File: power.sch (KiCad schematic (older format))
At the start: 40 parts, among them J1 USB_B_Mini, U1 USBLC6-2SC6, U2 BQ24190, U4 LP38691SD-3.3

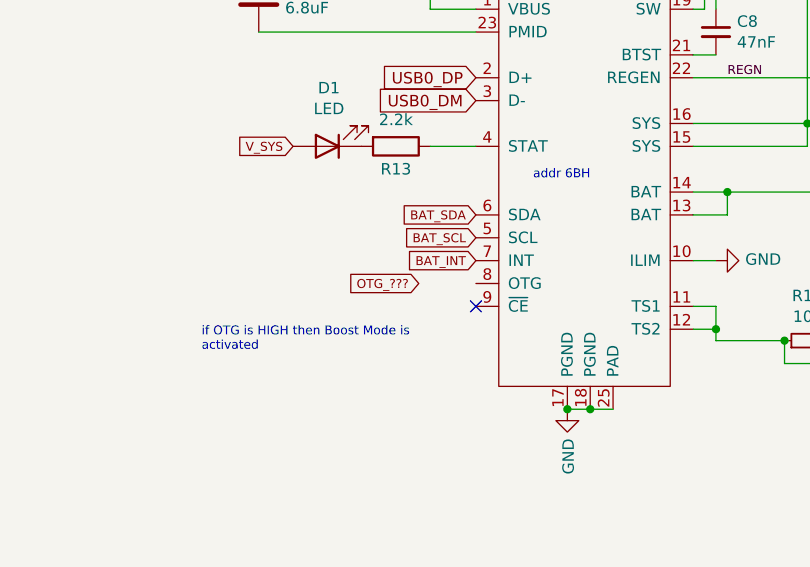
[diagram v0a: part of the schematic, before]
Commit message: Wire the OTG pin
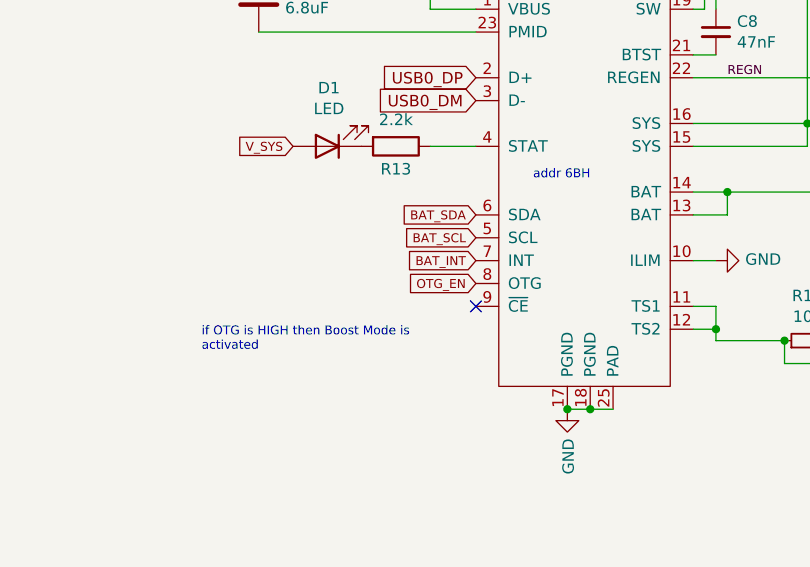
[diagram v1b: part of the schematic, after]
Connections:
- net OTG_EN: now reaches U2.8 (OTG)
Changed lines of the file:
@@
 	1900 10900 1800 10900
 Connection ~ 1800 10900
-Text GLabel 6000 5050 0    39   Input ~ 0
-OTG_???
+Text GLabel 6250 5050 0    39   Input ~ 0
+OTG_EN
 $EndSCHEMATC

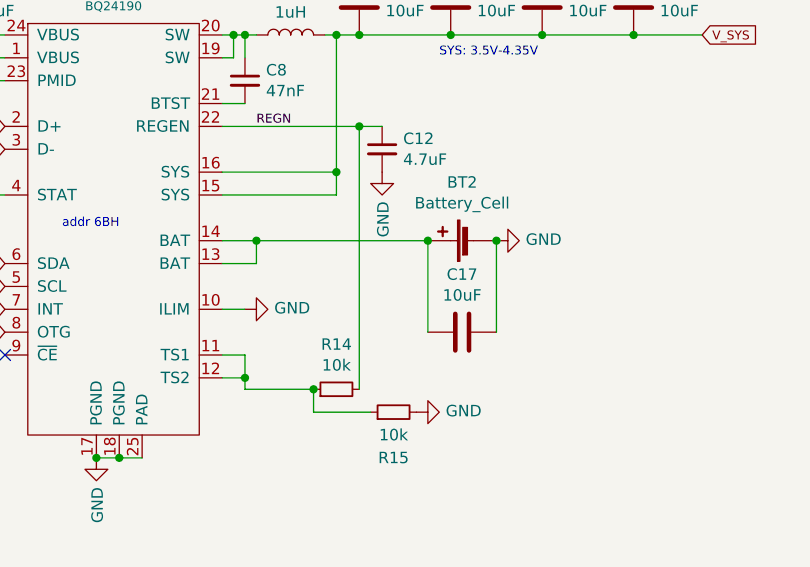
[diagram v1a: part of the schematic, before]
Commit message: Add TPs
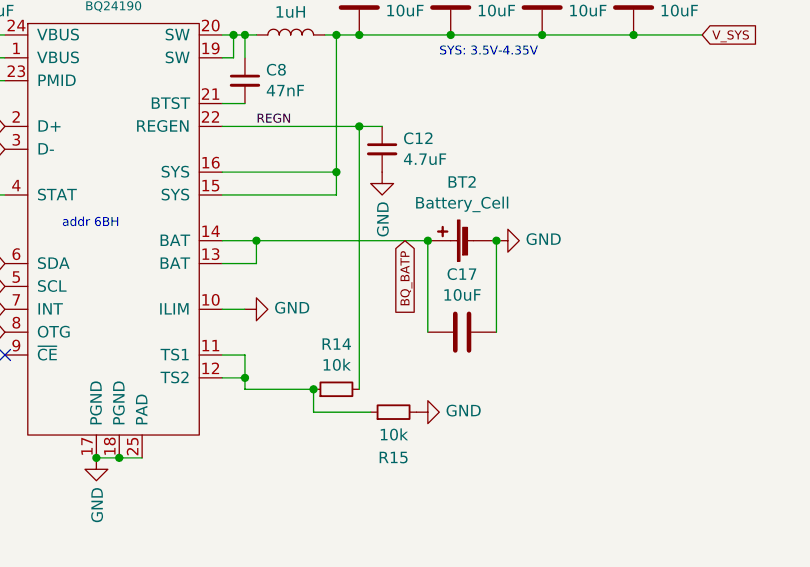
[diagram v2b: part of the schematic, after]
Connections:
- net BQ_BATP: now reaches BT2.1 (+), C17.2, U2.13 (BAT), U2.14 (BAT)
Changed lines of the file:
@@
 Text GLabel 6250 5050 0    39   Input ~ 0
 OTG_EN
+Text GLabel 8000 4650 3    39   Input ~ 0
+BQ_BATP
 $EndSCHEMATC

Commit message: Use libs; start assigning footprints
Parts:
- BT2: footprint (none) -> Connector_JST:JST_PH_B2B-PH-K_1x02_P2.00mm_Vertical
- J1: footprint (none) -> Connector_USB:USB_Mini-B_Wuerth_65100516121_Horizontal
- U1: footprint Package_TO_SOT_SMD:SOT-23-6 -> Package_TO_SOT_SMD:SOT-23-6_Handsoldering
- U2: footprint (none) -> Package_DFN_QFN:VQFN-24-1EP_4x4mm_P0.5mm_EP2.45x2.45mm_ThermalVias
- U4: footprint Package_QFP:LQFP-144_20x20mm_P0.5mm -> Package_SON:WSON-6-1EP_3x3mm_P0.95mm
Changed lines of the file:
@@
 F 0 "J1" H 1157 4867 50  0000 C CNN
 F 1 "USB_B_Mini" H 1157 4776 50  0000 C CNN
-F 2 "" H 1250 4350 50  0001 C CNN
+F 2 "Connector_USB:USB_Mini-B_Wuerth_65100516121_Horizontal" H 1250 4350 50  0001 C CNN
 F 3 "~" H 1250 4350 50  0001 C CNN
 	1    1100 4400
@@
 F 0 "U4" H 7300 1692 50  0000 C CNN
 F 1 "LP38691SD-3.3" H 7300 1601 50  0000 C CNN
-F 2 "Package_QFP:LQFP-144_20x20mm_P0.5mm" H 7300 1350 50  0001 C CNN
+F 2 "Package_SON:WSON-6-1EP_3x3mm_P0.95mm" H 7300 1350 50  0001 C CNN
 F 3 "https://www.nxp.com/docs/en/data-sheet/K66P144M180SF5V2.pdf" H 7300 1350 50  0001 C CNN
 	1    7300 1350
@@
 F 0 "U1" V 3150 4300 50  0000 L CNN
 F 1 "USBLC6-2SC6" V 2150 4150 50  0000 L CNN
-F 2 "Package_TO_SOT_SMD:SOT-23-6" H 2650 3950 50  0001 C CNN
+F 2 "Package_TO_SOT_SMD:SOT-23-6_Handsoldering" H 2650 3950 50  0001 C CNN
 F 3 "https://www.st.com/resource/en/datasheet/usblc6-2.pdf" H 2850 4800 50  0001 C CNN
 	1    2650 4450
@@
 F 0 "U2" H 6725 3751 39  0000 C CNN
 F 1 "BQ24190" H 6725 3676 39  0000 C CNN
-F 2 "" H 5700 3950 39  0001 C CNN
+F 2 "Package_DFN_QFN:VQFN-24-1EP_4x4mm_P0.5mm_EP2.45x2.45mm_ThermalVias" H 5700 3950 39  0001 C CNN
 F 3 "" H 5700 3950 39  0001 C CNN
 	1    6750 3650
@@
 F 0 "BT2" V 8555 4700 50  0000 C CNN
 F 1 "Battery_Cell" V 8464 4700 50  0000 C CNN
-F 2 "" V 8300 4710 50  0001 C CNN
+F 2 "Connector_JST:JST_PH_B2B-PH-K_1x02_P2.00mm_Vertical" V 8300 4710 50  0001 C CNN
 F 3 "~" V 8300 4710 50  0001 C CNN
 	1    8300 4650

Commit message: Assigning footprints
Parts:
- removed D2, D3: 1A, symbol Device:D_Schottky
- BT1: footprint (none) -> Battery:BatteryHolder_Keystone_1060_1x2032; mouser (none) -> 534-1060TR
- C1, C11, C12, C13, C15, C16, C17, C18, C19, C2, C20, C21, C22, C23, C24, C25, C26, C4, C5, C6, C7, C8, C9: footprint (none) -> Capacitor_SMD:C_0805_2012Metric_Pad1.18x1.45mm_HandSolder
- F1: footprint (none) -> Fuse:Fuse_0805_2012Metric_Pad1.15x1.40mm_HandSolder; mouser (none) -> 576-0805L020YR
- JP1: footprint (none) -> Jumper:SolderJumper-3_P1.3mm_Bridged2Bar12_Pad1.0x1.5mm_NumberLabels
- L1: footprint (none) -> Inductor_SMD:L_0805_2012Metric_Pad1.05x1.20mm_HandSolder; mouser (none) -> 704-MCQ1V2012-1R0-R
- R1, R13, R14, R15, R6: footprint (none) -> Resistor_SMD:R_0805_2012Metric_Pad1.20x1.40mm_HandSolder
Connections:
- net at C5.1, U4.1 (IN), U4.6 (IN): now also F1.1
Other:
- moved on the sheet: F1

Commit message: Finish led magic
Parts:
- D1: footprint (none) -> LED_SMD:LED_0603_1608Metric_Pad1.05x0.95mm_HandSolder; mouser (none) -> 859-LTST-C190GKT
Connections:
- net V_SYS: now also R13.2; no longer D1.2 (A)
- net at U2.4 (STAT): now also D1.1 (K); no longer R13.1
- new net: D1.2 (A), R13.1
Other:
- moved on the sheet: D1, R13
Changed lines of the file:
@@
 L Device:LED D?
 U 1 1 60D3B575
-P 5600 4450
+P 5750 4450
 AR Path="/5F7C29DF/60D3B575" Ref="D?"  Part="1"
 AR Path="/60CFD8F5/60D3B575" Ref="D1"  Part="1"
-F 0 "D1" H 5593 4195 50  0000 C CNN
-F 1 "LED" H 5593 4286 50  0000 C CNN
-F 2 "" H 5600 4450 50  0001 C CNN
-F 3 "~" H 5600 4450 50  0001 C CNN
-	1    5600 4450
+F 0 "D1" H 5743 4195 50  0000 C CNN
+F 1 "LED" H 5743 4286 50  0000 C CNN
+F 2 "LED_SMD:LED_0603_1608Metric_Pad1.05x0.95mm_HandSolder" H 5750 4450 50  0001 C CNN
+F 3 "~" H 5750 4450 50  0001 C CNN
+F 4 "859-LTST-C190GKT" H 5750 4450 50  0001 C CNN "mouser"
+	1    5750 4450
 	-1   0    0    1
 $EndComp
-Text GLabel 5450 4450 0    39   Input ~ 0
+Text GLabel 5300 4450 0    39   Input ~ 0
 V_SYS
 $Comp
 L Device:R R?
 U 1 1 60D3B57C
-P 5900 4450
+P 5450 4450
 AR Path="/5F7C29DF/60D3B57C" Ref="R?"  Part="1"
 AR Path="/60CFD8F5/60D3B57C" Ref="R13"  Part="1"
-F 0 "R13" V 6000 4450 50  0000 C CNN
-F 1 "2.2k" V 5784 4450 50  0000 C CNN
-F 2 "Resistor_SMD:R_0805_2012Metric_Pad1.20x1.40mm_HandSolder" V 5830 4450 50  0001 C CNN
-F 3 "~" H 5900 4450 50  0001 C CNN
-	1    5900 4450
+F 0 "R13" V 5550 4450 50  0000 C CNN
+F 1 "2.2k" V 5334 4450 50  0000 C CNN
+F 2 "Resistor_SMD:R_0805_2012Metric_Pad1.20x1.40mm_HandSolder" V 5380 4450 50  0001 C CNN
+F 3 "~" H 5450 4450 50  0001 C CNN
+	1    5450 4450
 	0    1    1    0
 $EndComp
 Wire Wire Line
-	6050 4450 6250 4450
+	5900 4450 6250 4450
 Wire Wire Line
 	7200 4750 7350 4750

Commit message: Switch keyboard matrix input to a mcp23017
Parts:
- U1: lcsc (none) -> C7519
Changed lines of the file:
@@
 F 2 "Package_TO_SOT_SMD:SOT-23-6_Handsoldering" H 2650 3950 50  0001 C CNN
 F 3 "https://www.st.com/resource/en/datasheet/usblc6-2.pdf" H 2850 4800 50  0001 C CNN
+F 4 "C7519" H 2650 4450 50  0001 C CNN "lcsc"
 	1    2650 4450
 	0    1    -1   0

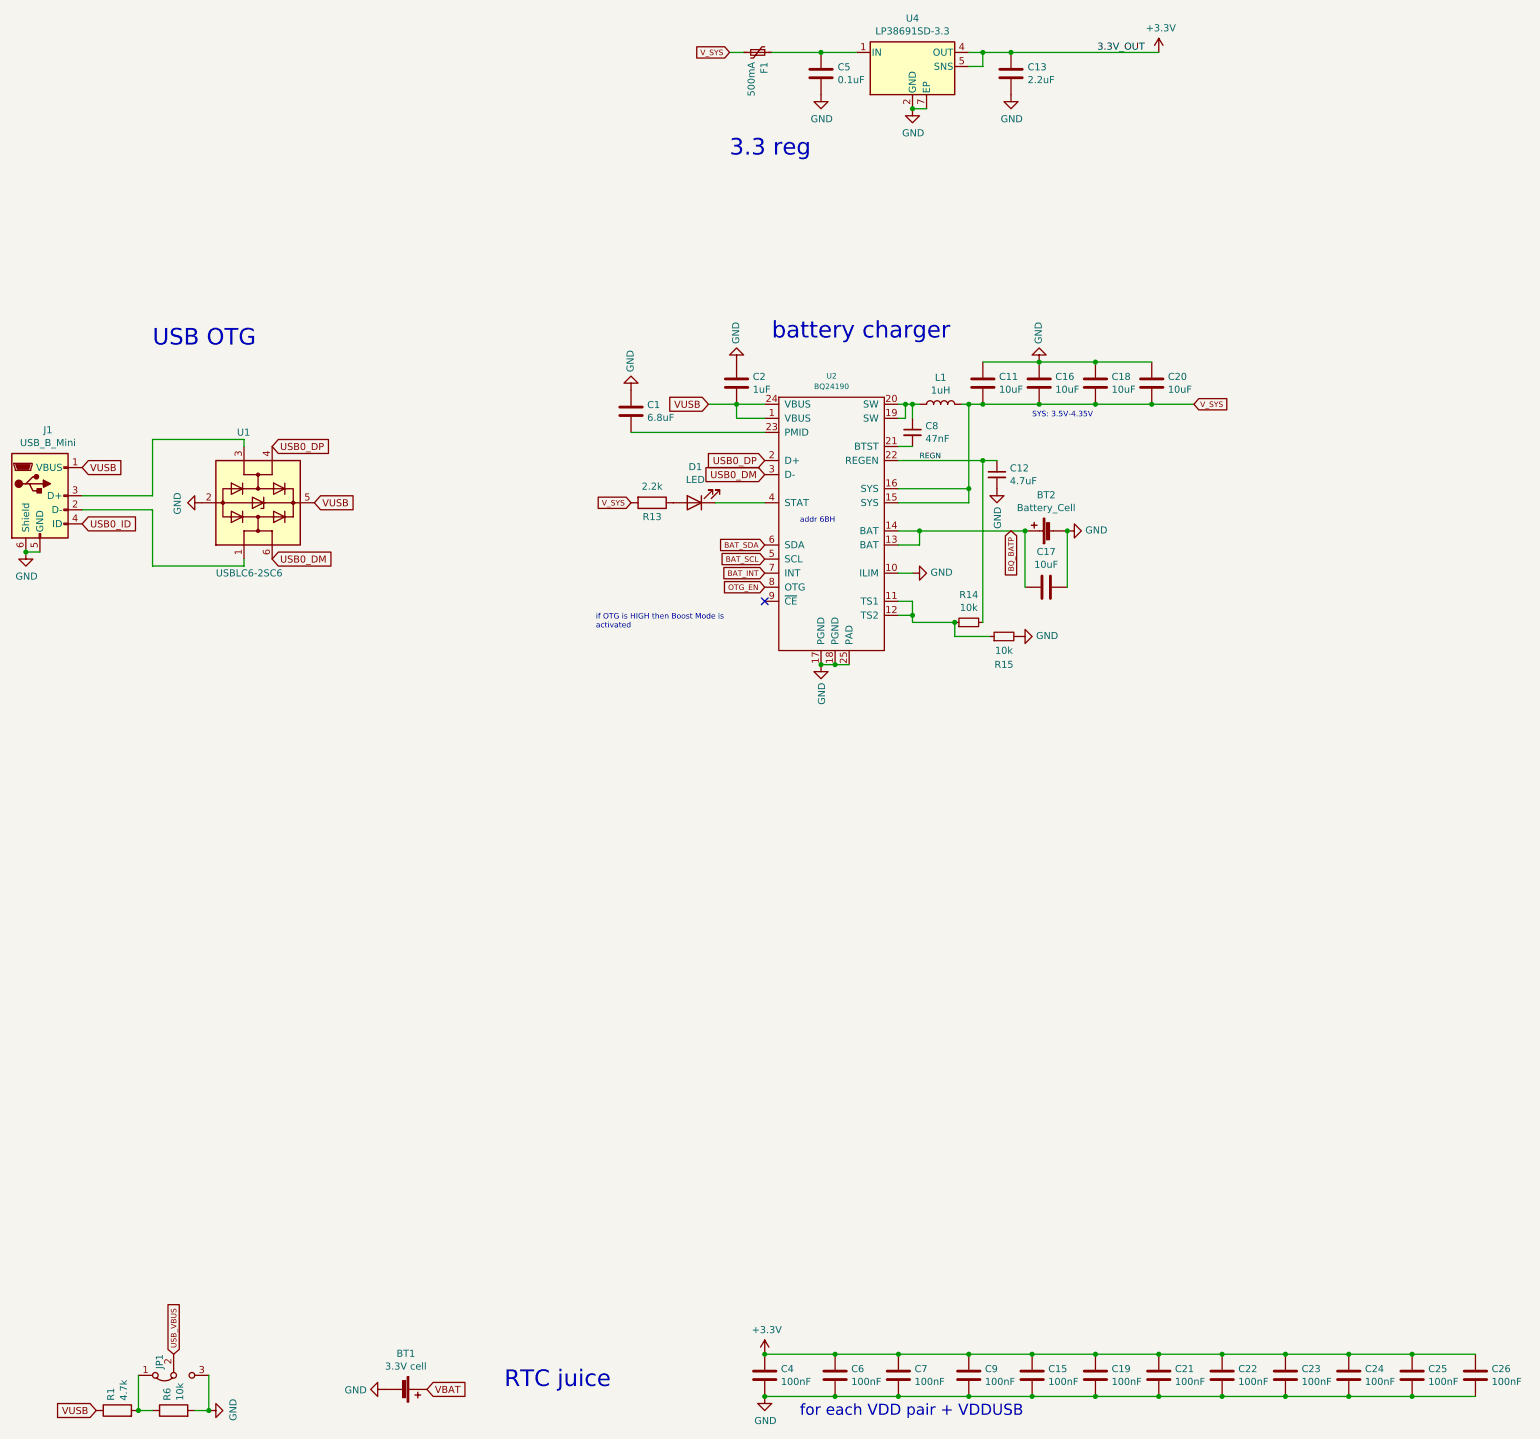
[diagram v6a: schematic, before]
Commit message: Switch stuff around; Use two MCP
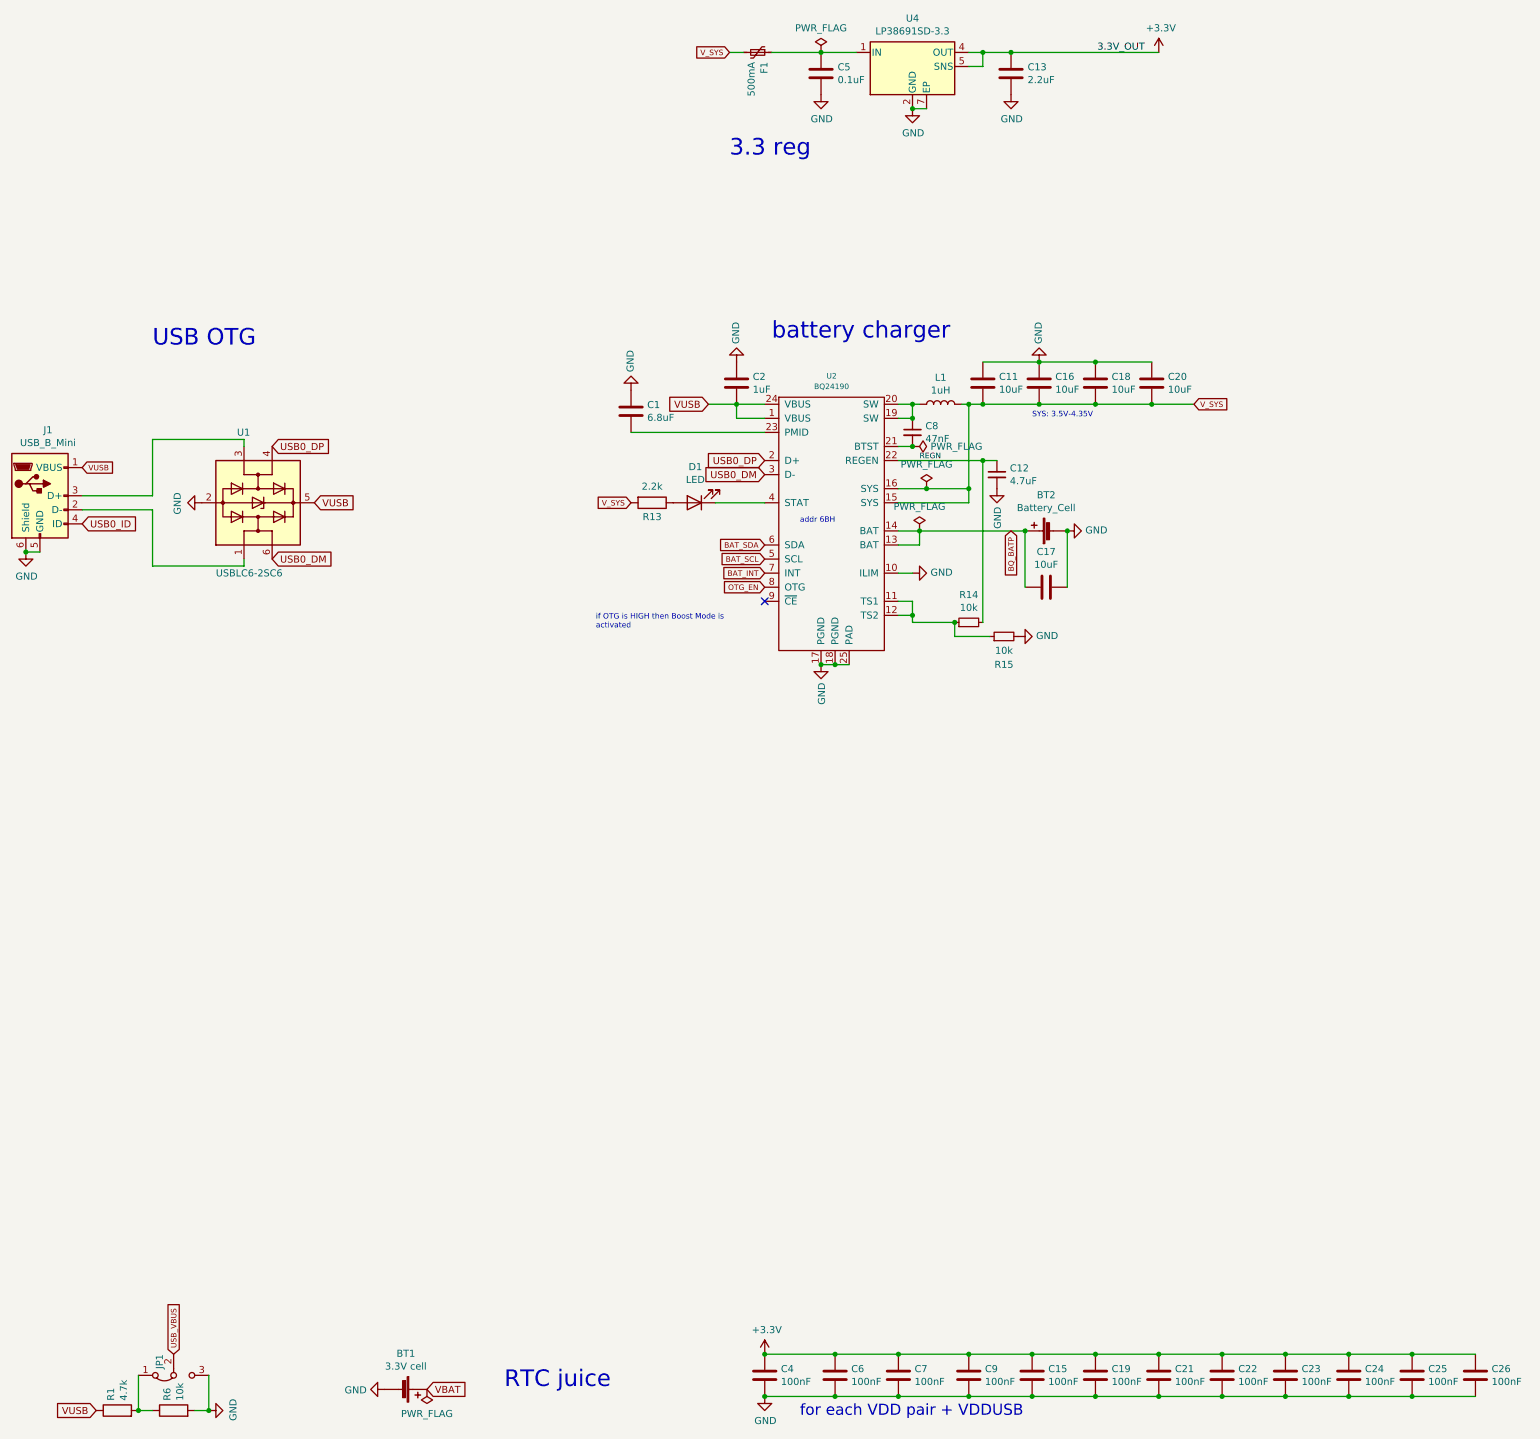
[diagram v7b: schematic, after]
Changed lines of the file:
@@
 $EndComp
-Wire Wire Line
-	6650 1250 6900 1250
 Wire Wire Line
 	7700 1350 7800 1350
 Wire Wire Line
 	7800 1350 7800 1250
-Wire Wire Line
-	7800 1250 7700 1250
-Wire Wire Line
-	7800 1250 8000 1250
 Connection ~ 7800 1250
 Connection ~ 8000 1250
@@
 	1000 4800 1100 4800
 Connection ~ 1000 4800
-Text GLabel 1400 4200 2    50   Input ~ 0
-VUSB
 Text GLabel 5850 3750 0    50   Input ~ 0
 VUSB
@@
 	1    0    0    -1
 $EndComp
-Wire Wire Line
-	5850 3750 6050 3750
 Connection ~ 6050 3750
 $Comp
@@
 	9000 3750 8600 3750
 Wire Wire Line
-	7350 3750 7300 3750
-Wire Wire Line
 	9000 3450 8600 3450
 Connection ~ 8200 3450
@@
 Text GLabel 6000 1250 0    39   Input ~ 0
 V_SYS
-$Comp
-L Device:C_Small C?
-U 1 1 60D3B51D
-P 7300 3950
-AR Path="/5F7C29DF/60D3B51D" Ref="C?"  Part="1"
-AR Path="/60CFD8F5/60D3B51D" Ref="C8"  Part="1"
-F 0 "C8" H 7392 3996 50  0000 L CNN
-F 1 "47nF" H 7392 3905 50  0000 L CNN
-F 2 "Capacitor_SMD:C_0805_2012Metric_Pad1.18x1.45mm_HandSolder" H 7300 3950 50  0001 C CNN
-F 3 "~" H 7300 3950 50  0001 C CNN
-	1    7300 3950
-	1    0    0    -1
-$EndComp
-Wire Wire Line
-	7300 3850 7300 3750
-Connection ~ 7300 3750
-Wire Wire Line
-	7300 3750 7250 3750
 Wire Wire Line
 	7200 4050 7300 4050
@@
 $EndComp
 Wire Wire Line
-	7200 4350 7700 4350
+	7200 4350 7400 4350
 Wire Wire Line
 	7700 4350 7700 3750
@@
 Wire Wire Line
 	7700 3750 7650 3750
-Wire Wire Line
-	7200 3850 7250 3850
-Wire Wire Line
-	7250 3850 7250 3750
-Connection ~ 7250 3750
-Wire Wire Line
-	7250 3750 7200 3750
 Wire Wire Line
 	7200 4450 7700 4450
@@
 Wire Wire Line
 	6050 3750 6250 3750
-Wire Wire Line
-	6250 3850 6050 3850
 Wire Wire Line
 	6050 3850 6050 3750
@@
 	6300 1250 6650 1250
 Connection ~ 6650 1250
+Wire Wire Line
+	7800 1250 8000 1250
+Wire Wire Line
+	7800 1250 7700 1250
+Wire Wire Line
+	5850 3750 6050 3750
+$Comp
+L power:PWR_FLAG #FLG0107
+U 1 1 6185E135
+P 3850 10750
+F 0 "#FLG0107" H 3850 10825 50  0001 C CNN
+F 1 "PWR_FLAG" H 3850 10923 50  0000 C CNN
+F 2 "" H 3850 10750 50  0001 C CNN
+F 3 "~" H 3850 10750 50  0001 C CNN
+	1    3850 10750
+	-1   0    0    1
+$EndComp
+$Comp
+L power:PWR_FLAG #FLG0108
+U 1 1 6185F480
+P 7400 4350
+F 0 "#FLG0108" H 7400 4425 50  0001 C CNN
+F 1 "PWR_FLAG" H 7400 4523 50  0000 C CNN
+F 2 "" H 7400 4350 50  0001 C CNN
+F 3 "~" H 7400 4350 50  0001 C CNN
+	1    7400 4350
+	1    0    0    -1
+$EndComp
+Connection ~ 7400 4350
+Wire Wire Line
+	7400 4350 7700 4350
+$Comp
+L power:PWR_FLAG #FLG0109
+U 1 1 618606ED
+P 7350 4650
+F 0 "#FLG0109" H 7350 4725 50  0001 C CNN
+F 1 "PWR_FLAG" H 7350 4823 50  0000 C CNN
+F 2 "" H 7350 4650 50  0001 C CNN
+F 3 "~" H 7350 4650 50  0001 C CNN
+	1    7350 4650
+	1    0    0    -1
+$EndComp
+Wire Wire Line
+	6650 1250 6900 1250
+$Comp
+L power:PWR_FLAG #FLG0103
+U 1 1 6186631C
+P 6650 1250
+F 0 "#FLG0103" H 6650 1325 50  0001 C CNN
+F 1 "PWR_FLAG" H 6650 1423 50  0000 C CNN
+F 2 "" H 6650 1250 50  0001 C CNN
+F 3 "~" H 6650 1250 50  0001 C CNN
+	1    6650 1250
+	1    0    0    -1
+$EndComp
+Text GLabel 1400 4200 2    39   Input ~ 0
+VUSB
+Wire Wire Line
+	6050 3850 6250 3850
+$Comp
+L Device:C_Small C?
+U 1 1 60D3B51D
+P 7300 3950
+AR Path="/5F7C29DF/60D3B51D" Ref="C?"  Part="1"
+AR Path="/60CFD8F5/60D3B51D" Ref="C8"  Part="1"
+F 0 "C8" H 7392 3996 50  0000 L CNN
+F 1 "47nF" H 7392 3905 50  0000 L CNN
+F 2 "Capacitor_SMD:C_0805_2012Metric_Pad1.18x1.45mm_HandSolder" H 7300 3950 50  0001 C CNN
+F 3 "~" H 7300 3950 50  0001 C CNN
+	1    7300 3950
+	1    0    0    -1
+$EndComp
+Wire Wire Line
+	7200 3850 7300 3850
+Wire Wire Line
+	7200 3750 7300 3750
+Wire Wire Line
+	7300 3850 7300 3750
+Connection ~ 7300 3850
+Connection ~ 7300 3750
+Wire Wire Line
+	7300 3750 7350 3750
+Connection ~ 7300 4050
+$Comp
+L power:PWR_FLAG #FLG0102
+U 1 1 6184D393
+P 7300 4050
+F 0 "#FLG0102" H 7300 4125 50  0001 C CNN
+F 1 "PWR_FLAG" V 7300 4178 50  0000 L CNN
+F 2 "" H 7300 4050 50  0001 C CNN
+F 3 "~" H 7300 4050 50  0001 C CNN
+	1    7300 4050
+	0    1    1    0
+$EndComp
 $EndSCHEMATC
